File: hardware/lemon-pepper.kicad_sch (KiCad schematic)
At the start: 22 parts, among them J101 INPUT, M101 MOT

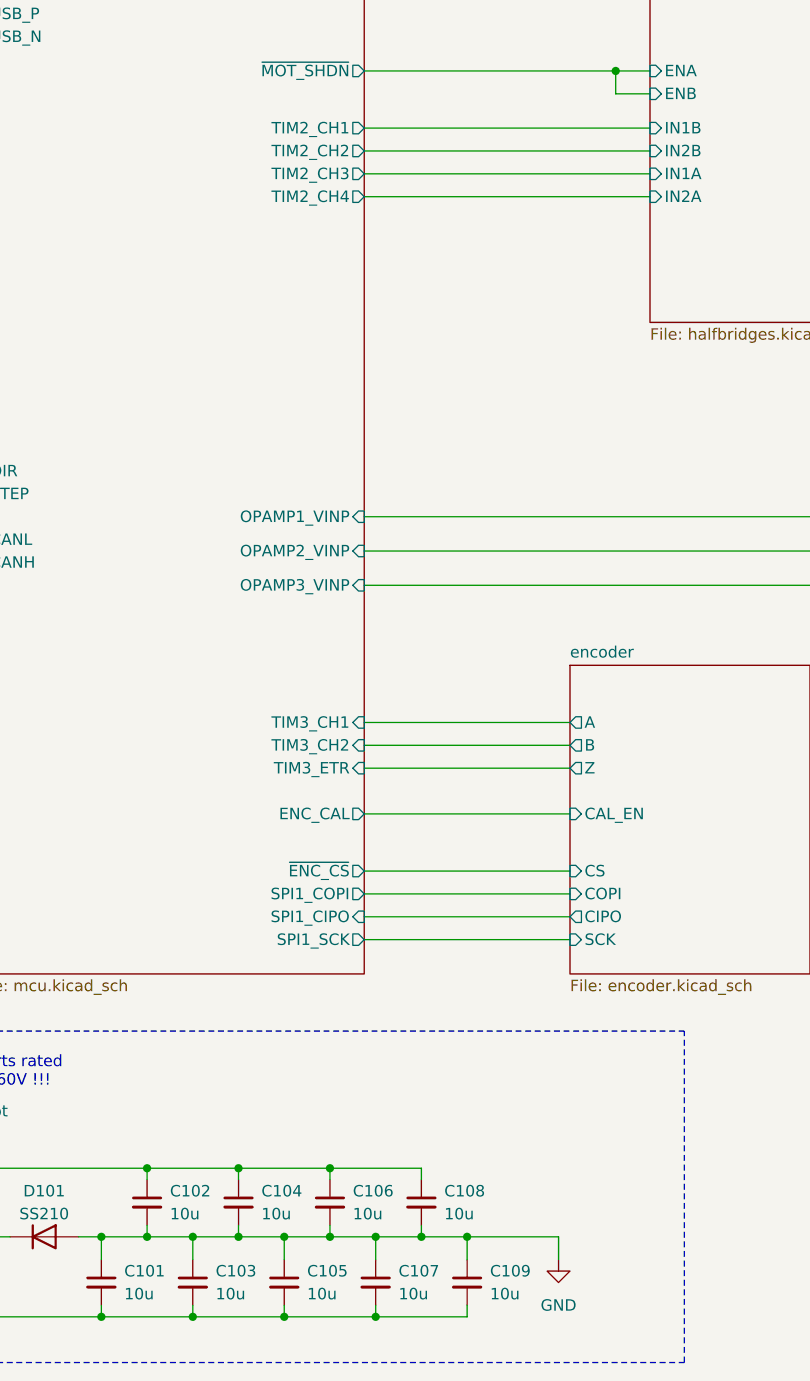
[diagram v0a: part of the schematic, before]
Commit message: add user button
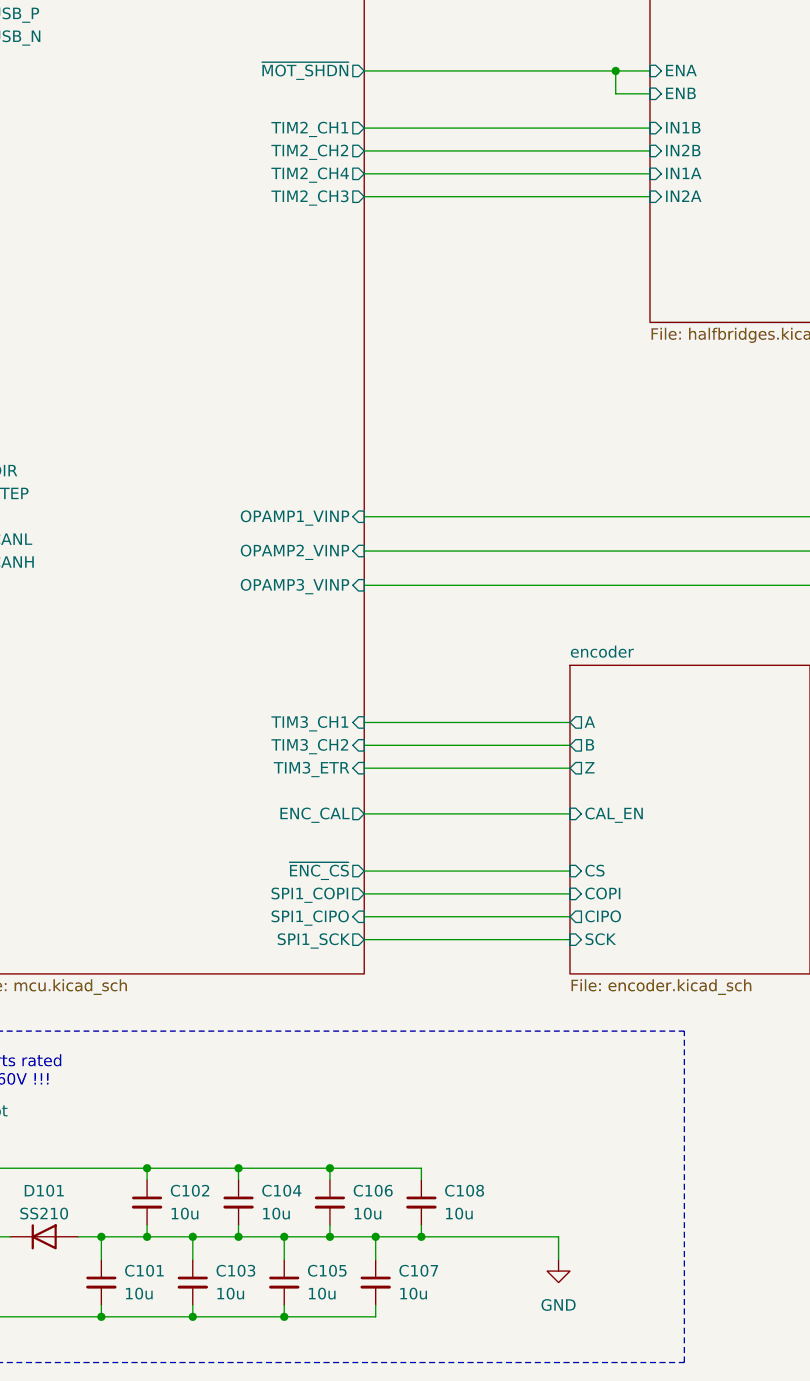
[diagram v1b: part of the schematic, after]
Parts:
- removed C109: 10u, Capacitor_SMD:C_0805_2012Metric, symbol Device:C_Small
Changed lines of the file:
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@@
   (junction (at 78.74 59.69) (diameter 0) (color 0 0 0 0)
   )
-  (junction (at 147.32 177.8) (diameter 0) (color 0 0 0 0)
-  )
   (junction (at 69.85 95.25) (diameter 0) (color 0 0 0 0)
   )
@@
   (junction (at 69.85 102.87) (diameter 0) (color 0 0 0 0)
   )
-  (junction (at 137.16 186.69) (diameter 0) (color 0 0 0 0)
-  )
   (junction (at 132.08 170.18) (diameter 0) (color 0 0 0 0)
   )
@@
     (stroke (width 0) (type default))
   )
-  (wire (pts (xy 147.32 186.69) (xy 147.32 185.42))
-    (stroke (width 0) (type default))
-  )
   (wire (pts (xy 135.89 62.23) (xy 167.64 62.23))
     (stroke (width 0) (type default))
   )
-  (wire (pts (xy 147.32 180.34) (xy 147.32 177.8))
-    (stroke (width 0) (type default))
-  )
   (wire (pts (xy 271.78 138.43) (xy 271.78 144.78))
     (stroke (width 0) (type default))
@@
   )
   (wire (pts (xy 240.03 57.15) (xy 240.03 71.12))
-    (stroke (width 0) (type default))
-  )
-  (wire (pts (xy 137.16 186.69) (xy 147.32 186.69))
     (stroke (width 0) (type default))
   )
@@
     (stroke (width 0) (type dash))
   )
-  (wire (pts (xy 147.32 177.8) (xy 157.48 177.8))
+  (wire (pts (xy 142.24 177.8) (xy 157.48 177.8))
     (stroke (width 0) (type default))
   )
@@
   )
   (wire (pts (xy 62.23 59.69) (xy 67.31 59.69))
-    (stroke (width 0) (type default))
-  )
-  (wire (pts (xy 142.24 177.8) (xy 147.32 177.8))
     (stroke (width 0) (type default))
   )
@@
         (path "/0306e2fa-4433-4288-91d9-65a3484207ad"
           (reference "C107") (unit 1)
-        )
-      )
-    )
-  )
-  (symbol (lib_id "Device:C_Small") (at 147.32 182.88 0) (unit 1)
-    (in_bom yes) (on_board yes) (dnp no)
-    (property "Reference" "C109" (at 149.86 181.6163 0)
-      (effects (font (size 1.27 1.27)) (justify left))
-    )
-    (property "Value" "10u" (at 149.86 184.1563 0)
-      (effects (font (size 1.27 1.27)) (justify left))
-    )
-    (property "Footprint" "Capacitor_SMD:C_0805_2012Metric" (at 147.32 182.88 0)
-      (effects (font (size 1.27 1.27)) hide)
-    )
-    (property "Datasheet" "~" (at 147.32 182.88 0)
-      (effects (font (size 1.27 1.27)) hide)
-    )
-    (property "LCSC Part" "C440198" (at 147.32 182.88 0)
-      (effects (font (size 1.27 1.27)) hide)
-    )
-    (pin "1")
-    (pin "2")
-    (instances
-      (project "lemon-pepper"
-        (path "/0306e2fa-4433-4288-91d9-65a3484207ad"
-          (reference "C109") (unit 1)
         )
       )
@@
       (effects (font (size 1.27 1.27)) (justify left))
     )
-    (pin "TIM2_CH4" output (at 135.89 62.23 0)
-      (effects (font (size 1.27 1.27)) (justify right))
-    )
-    (pin "TIM2_CH3" output (at 135.89 59.69 0)
-      (effects (font (size 1.27 1.27)) (justify right))
-    )
+    (pin "TIM2_CH4" output (at 135.89 59.69 0)
+      (effects (font (size 1.27 1.27)) (justify right))
+    )
+    (pin "TIM2_CH3" output (at 135.89 62.23 0)
+      (effects (font (size 1.27 1.27)) (justify right))
+    )

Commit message: rev3 documentation
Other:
- sheet current sense ports: added none; removed W_SENSE
- sheet mcu ports: added none; removed OPAMP2_VINP
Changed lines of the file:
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@@
-    (stroke (width 0) (type default))
-  )
-  (wire (pts (xy 217.17 114.3) (xy 217.17 101.6))
     (stroke (width 0) (type default))
   )
@@
     (stroke (width 0) (type default))
   )
-  (wire (pts (xy 135.89 101.6) (xy 217.17 101.6))
-    (stroke (width 0) (type default))
-  )
   (wire (pts (xy 135.89 144.78) (xy 158.75 144.78))
     (stroke (width 0) (type default))
@@
     (stroke (width 0) (type default))
   )
-  (wire (pts (xy 213.36 114.3) (xy 213.36 105.41))
+  (wire (pts (xy 217.17 114.3) (xy 217.17 101.6))
     (stroke (width 0) (type default))
   )
@@
     (stroke (width 0) (type default))
   )
-  (wire (pts (xy 135.89 105.41) (xy 213.36 105.41))
+  (wire (pts (xy 135.89 101.6) (xy 217.17 101.6))
     (stroke (width 0) (type default))
   )
@@
       (effects (font (size 1.27 1.27)) (justify right))
     )
-    (pin "V_SENSE" output (at 213.36 114.3 90)
+    (pin "V_SENSE" output (at 217.17 114.3 90)
       (effects (font (size 1.27 1.27)) (justify right))
     )
     (pin "U_SENSE" output (at 220.98 114.3 90)
-      (effects (font (size 1.27 1.27)) (justify right))
-    )
-    (pin "W_SENSE" output (at 217.17 114.3 90)
       (effects (font (size 1.27 1.27)) (justify right))
     )
@@
       (effects (font (size 1.27 1.27)) (justify left))
     )
-    (pin "OPAMP2_VINP" input (at 135.89 101.6 0)
-      (effects (font (size 1.27 1.27)) (justify right))
-    )
     (pin "SPI1_SCK" output (at 135.89 144.78 0)
       (effects (font (size 1.27 1.27)) (justify right))
@@
       (effects (font (size 1.27 1.27)) (justify right))
     )
-    (pin "OPAMP3_VINP" input (at 135.89 105.41 0)
-      (effects (font (size 1.27 1.27)) (justify right))
-    )
+    (pin "OPAMP3_VINP" input (at 135.89 101.6 0)
+      (effects (font (size 1.27 1.27)) (justify right))
+    )

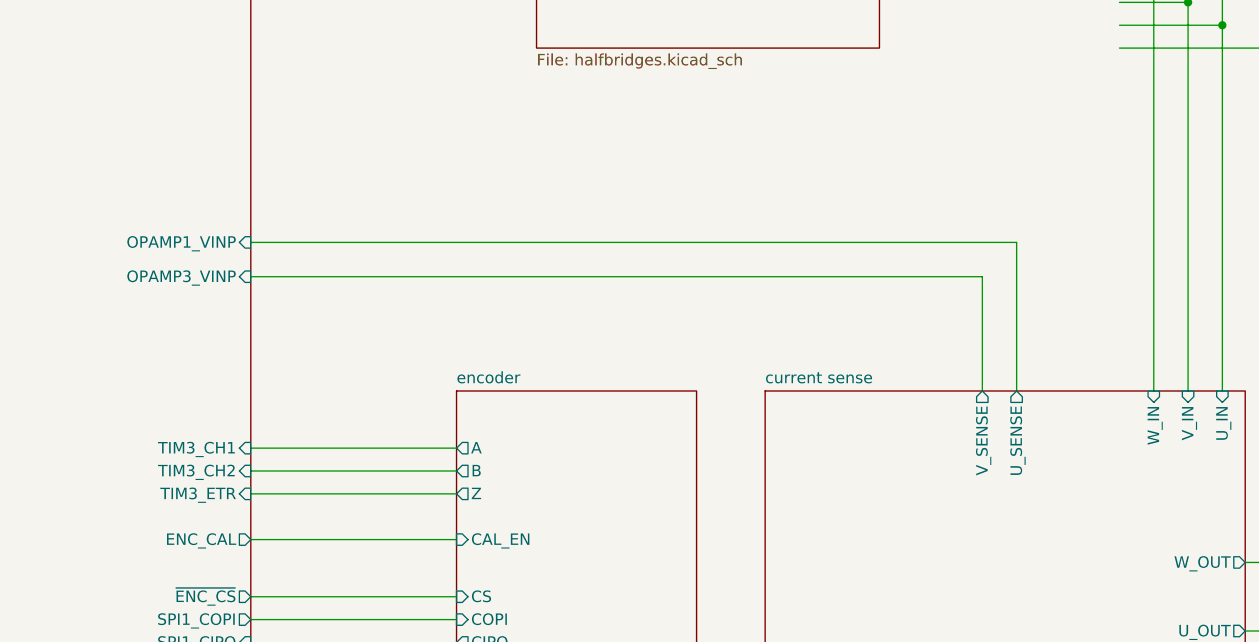
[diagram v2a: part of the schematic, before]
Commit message: Made analog gain of current sense amps selectable by mcu. Removed analog ground plane and tied all grounds together
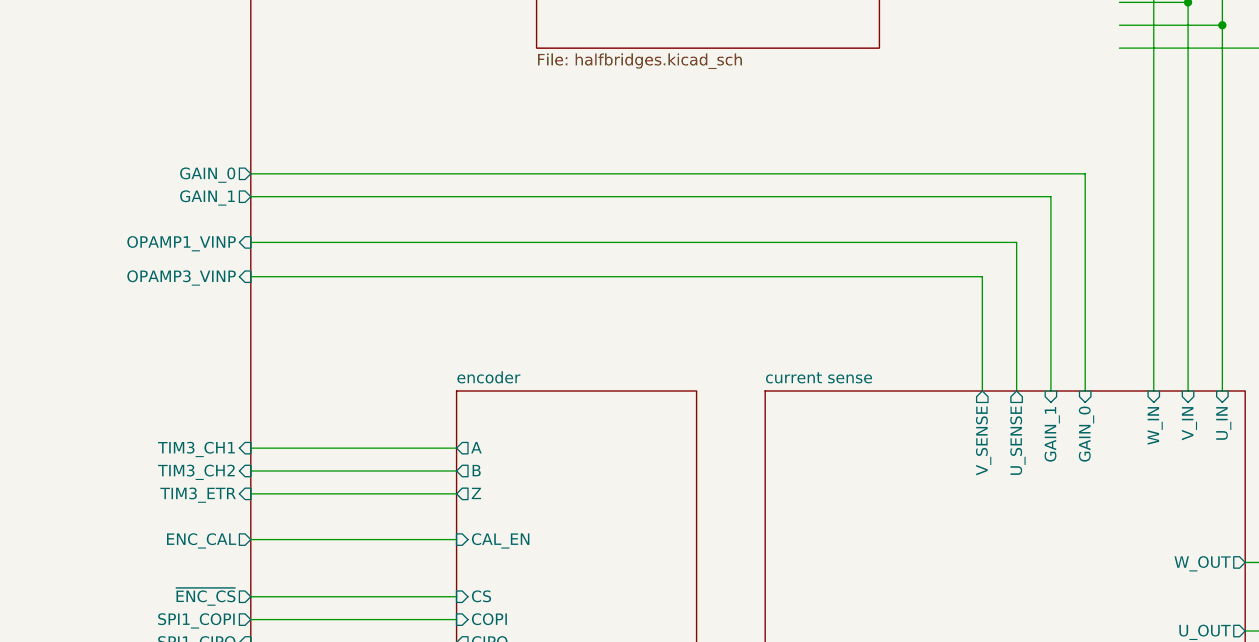
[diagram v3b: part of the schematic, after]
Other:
- sheet current sense ports: added GAIN_0, GAIN_1; removed none
- sheet mcu ports: added GAIN_0, GAIN_1; removed none
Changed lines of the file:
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@@
+    (stroke (width 0) (type default))
+  )
+  (wire (pts (xy 135.89 92.71) (xy 224.79 92.71))
     (stroke (width 0) (type default))
   )
@@
   )
   (wire (pts (xy 116.84 186.69) (xy 127 186.69))
+    (stroke (width 0) (type default))
+  )
+  (wire (pts (xy 228.6 114.3) (xy 228.6 90.17))
     (stroke (width 0) (type default))
   )
@@
     (stroke (width 0) (type default))
   )
+  (wire (pts (xy 224.79 92.71) (xy 224.79 114.3))
+    (stroke (width 0) (type default))
+  )
   (wire (pts (xy 111.76 170.18) (xy 111.76 171.45))
     (stroke (width 0) (type default))
@@
   )
   (wire (pts (xy 46.99 82.55) (xy 46.99 87.63))
+    (stroke (width 0) (type default))
+  )
+  (wire (pts (xy 228.6 90.17) (xy 135.89 90.17))
     (stroke (width 0) (type default))
   )
@@
       (effects (font (size 1.27 1.27)) (justify right))
     )
+    (pin "GAIN_1" input (at 224.79 114.3 90)
+      (effects (font (size 1.27 1.27)) (justify right))
+    )
+    (pin "GAIN_0" input (at 228.6 114.3 90)
+      (effects (font (size 1.27 1.27)) (justify right))
+    )
     (instances
       (project "lemon-pepper"
@@
       (effects (font (size 1.27 1.27)) (justify right))
     )
+    (pin "GAIN_0" output (at 135.89 90.17 0)
+      (effects (font (size 1.27 1.27)) (justify right))
+    )
+    (pin "GAIN_1" output (at 135.89 92.71 0)
+      (effects (font (size 1.27 1.27)) (justify right))
+    )

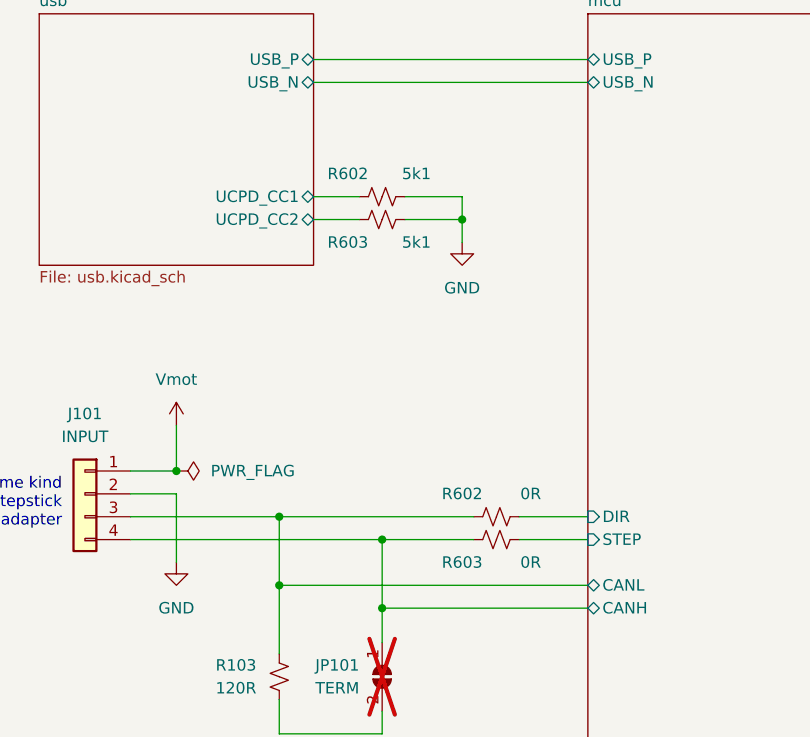
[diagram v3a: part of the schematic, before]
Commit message: Update firmware defines to match hardware
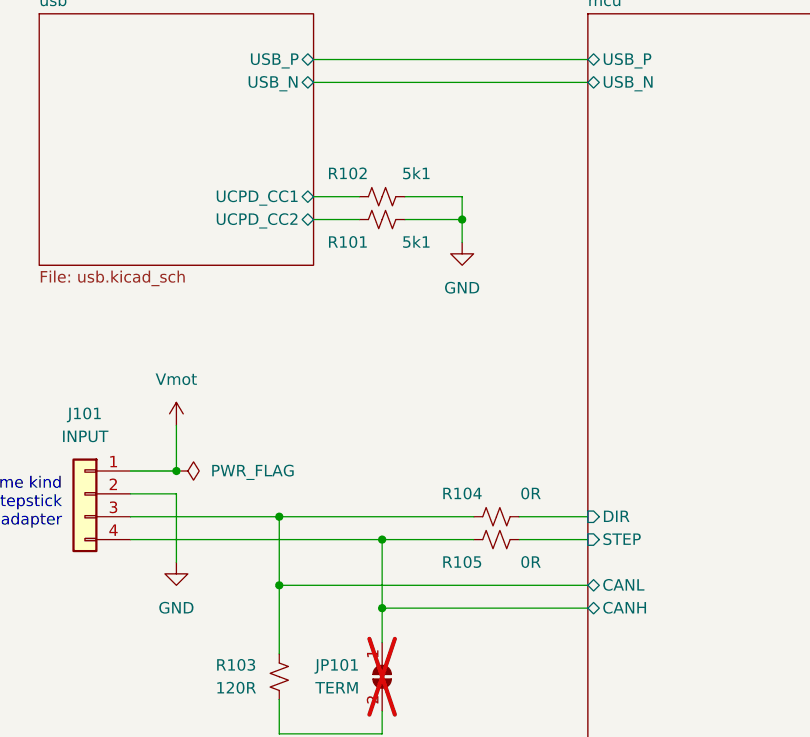
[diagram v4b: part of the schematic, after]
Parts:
- renumbered R603 to R101, R602 to R102, R602 to R104, R603 to R105
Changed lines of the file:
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@@
   (symbol (lib_id "Device:R_Small_US") (at 82.55 92.71 90) (unit 1)
     (in_bom yes) (on_board yes) (dnp no)
-    (property "Reference" "R602" (at 78.74 90.17 90)
+    (property "Reference" "R104" (at 78.74 90.17 90)
       (effects (font (size 1.27 1.27)))
     )
@@
     (instances
       (project "lemon-pepper"
-        (path "/0306e2fa-4433-4288-91d9-65a3484207ad/7f2d245a-6dca-4eb9-9839-7fdf255edd98"
-          (reference "R602") (unit 1)
-        )
         (path "/0306e2fa-4433-4288-91d9-65a3484207ad"
           (reference "R104") (unit 1)
@@
   (symbol (lib_id "Device:R_Small_US") (at 82.55 95.25 270) (unit 1)
     (in_bom yes) (on_board yes) (dnp no)
-    (property "Reference" "R603" (at 78.74 97.79 90)
+    (property "Reference" "R105" (at 78.74 97.79 90)
       (effects (font (size 1.27 1.27)))
     )
@@
     (instances
       (project "lemon-pepper"
-        (path "/0306e2fa-4433-4288-91d9-65a3484207ad/7f2d245a-6dca-4eb9-9839-7fdf255edd98"
-          (reference "R603") (unit 1)
-        )
         (path "/0306e2fa-4433-4288-91d9-65a3484207ad"
           (reference "R105") (unit 1)
@@
   (symbol (lib_id "Device:R_Small_US") (at 69.85 57.15 90) (unit 1)
     (in_bom yes) (on_board yes) (dnp no)
-    (property "Reference" "R602" (at 66.04 54.61 90)
+    (property "Reference" "R102" (at 66.04 54.61 90)
       (effects (font (size 1.27 1.27)))
     )
@@
     (instances
       (project "lemon-pepper"
-        (path "/0306e2fa-4433-4288-91d9-65a3484207ad/7f2d245a-6dca-4eb9-9839-7fdf255edd98"
-          (reference "R602") (unit 1)
-        )
         (path "/0306e2fa-4433-4288-91d9-65a3484207ad"
           (reference "R102") (unit 1)
@@
   (symbol (lib_id "Device:R_Small_US") (at 69.85 59.69 270) (unit 1)
     (in_bom yes) (on_board yes) (dnp no)
-    (property "Reference" "R603" (at 66.04 62.23 90)
+    (property "Reference" "R101" (at 66.04 62.23 90)
       (effects (font (size 1.27 1.27)))
     )
@@
     (instances
       (project "lemon-pepper"
-        (path "/0306e2fa-4433-4288-91d9-65a3484207ad/7f2d245a-6dca-4eb9-9839-7fdf255edd98"
-          (reference "R603") (unit 1)
-        )
         (path "/0306e2fa-4433-4288-91d9-65a3484207ad"
           (reference "R101") (unit 1)

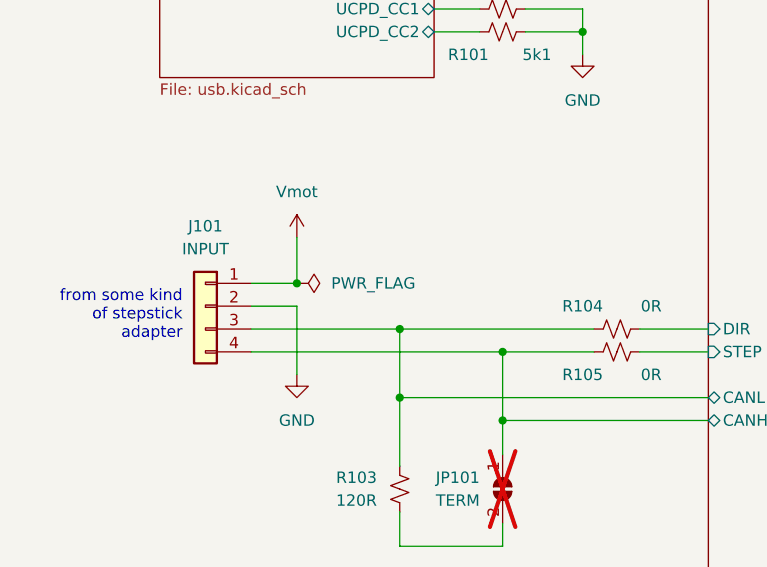
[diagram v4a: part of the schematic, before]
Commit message: fix erc failures
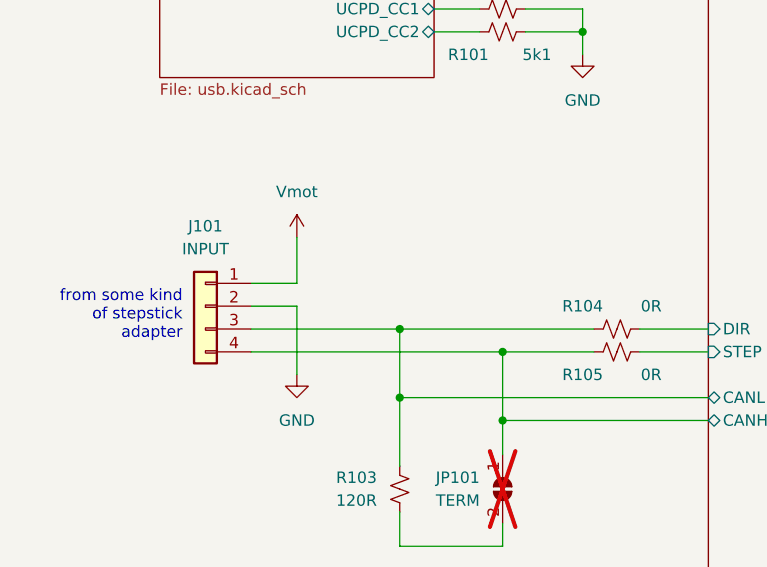
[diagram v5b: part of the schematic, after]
